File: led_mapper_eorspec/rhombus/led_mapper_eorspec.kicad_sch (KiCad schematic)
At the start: 1 part, among them J1 Conn_02x12_Top_Bottom

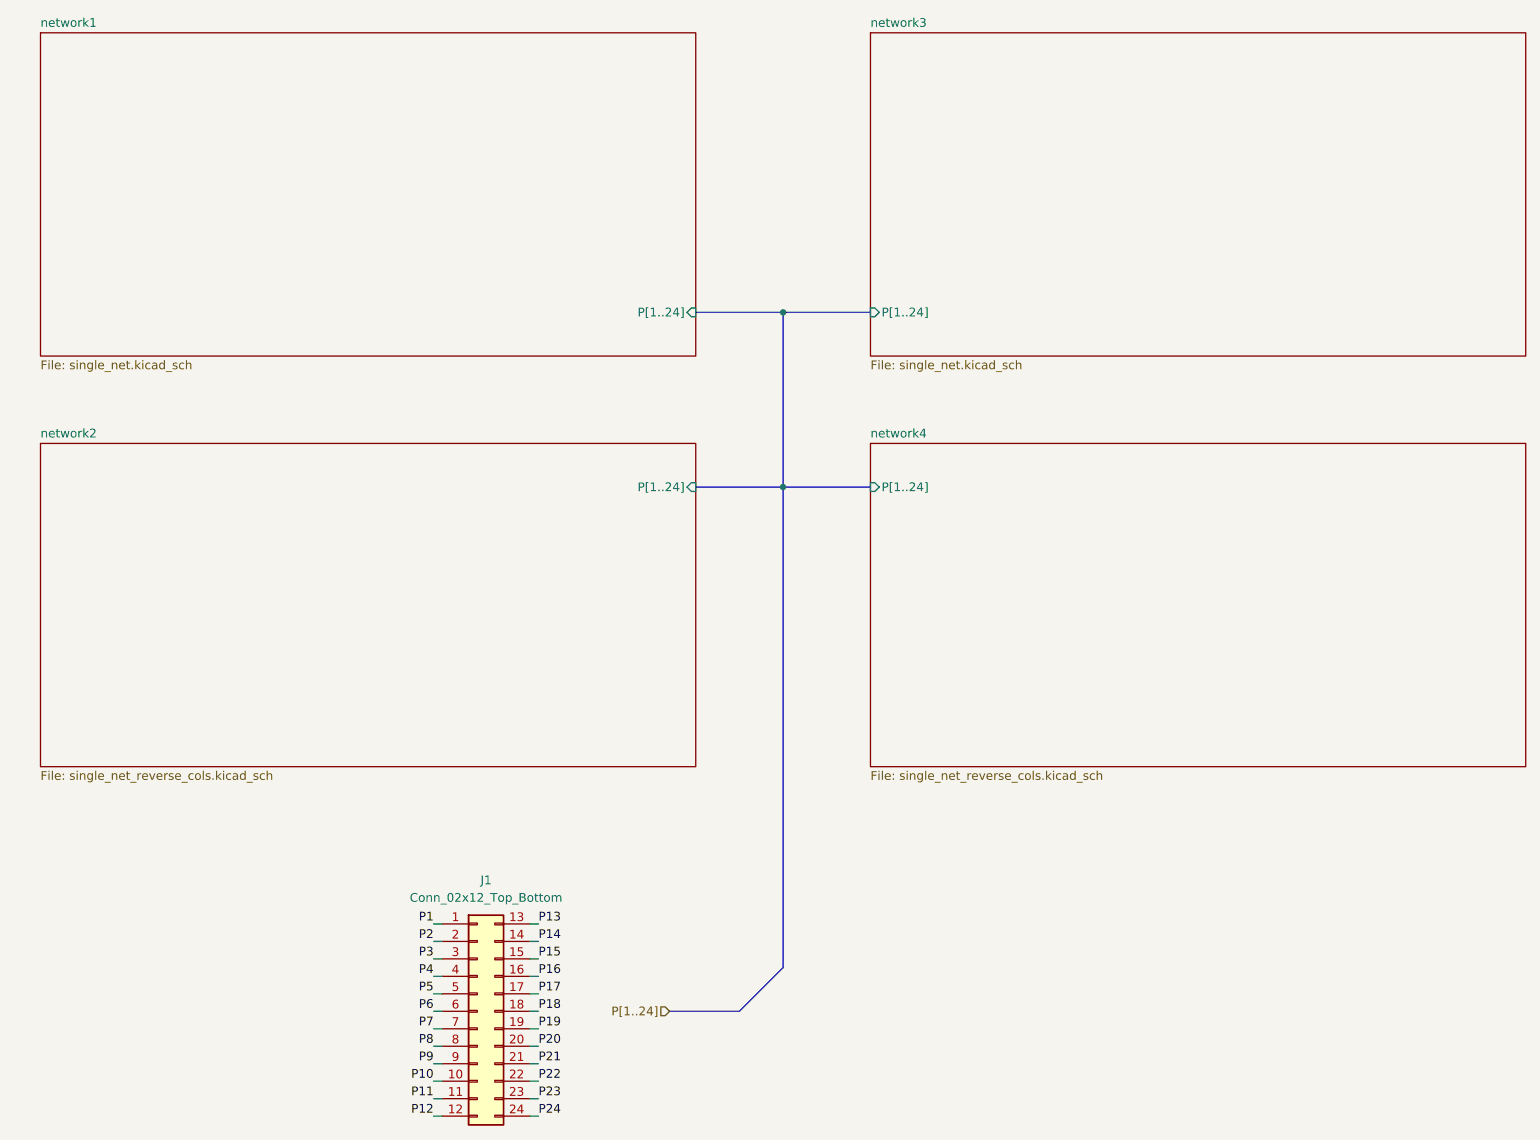
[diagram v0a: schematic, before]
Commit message: Complete single-net schematic, led placement and vertical tracks
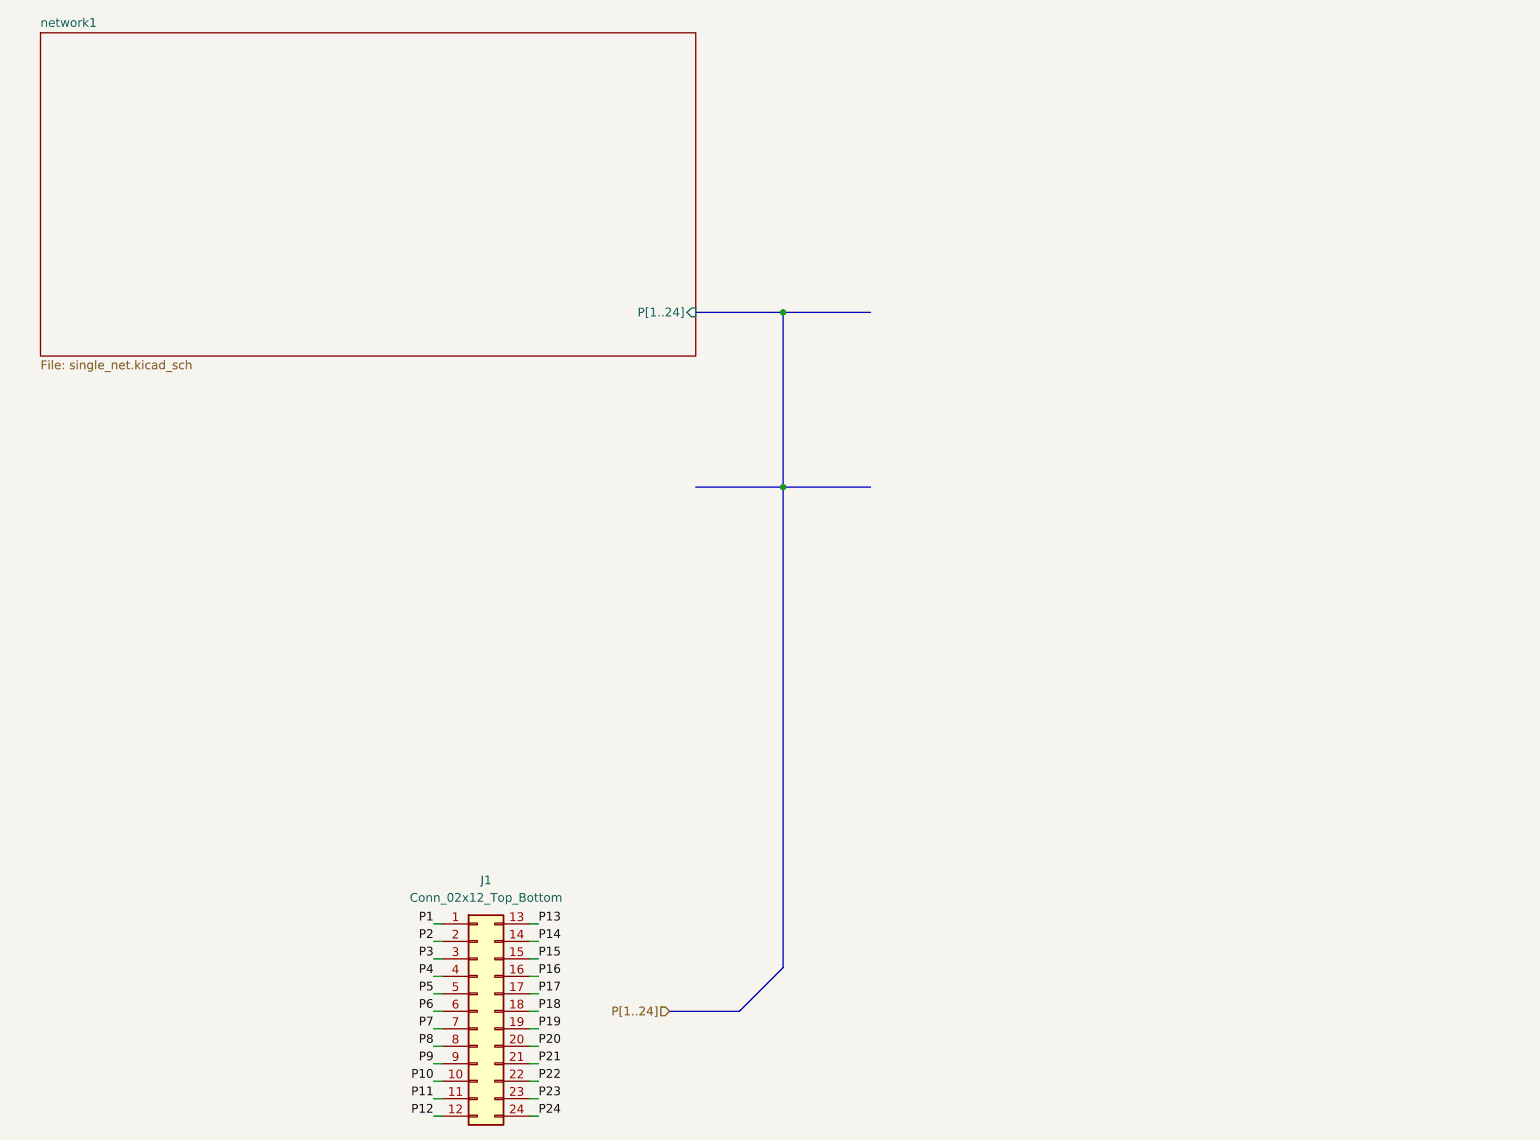
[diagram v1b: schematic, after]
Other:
- removed sheet network2
- removed sheet network3
- removed sheet network4
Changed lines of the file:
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@@
 (kicad_sch
-	(version 20231120)
+	(version 20260306)
 	(generator "eeschema")
-	(generator_version "8.0")
+	(generator_version "10.0")
 	(paper "A4")
 	(junction
@@
 		(at 107.95 171.45 0)
 		(unit 1)
+		(body_style 1)
+		(exclude_from_sim no)
+		(in_bom yes)
+		(on_board yes)
+		(in_pos_files yes)
+		(dnp no)
+		(fields_autoplaced yes)
+		(property "Reference" "J1"
+			(at 109.22 152.4 0)
+			(show_name no)
+			(do_not_autoplace no)
+			(effects
+				(font
+					(size 1.27 1.27)
+				)
+			)
+		)
+		(property "Value" "Conn_02x12_Top_Bottom"
+			(at 109.22 154.94 0)
+			(show_name no)
+			(do_not_autoplace no)
+			(effects
+				(font
+					(size 1.27 1.27)
+				)
+			)
+		)
+		(property "Footprint" "ccatlib:PinSocket_2x12_P2.54mm_Vertical_SMD_custom"
+			(at 107.95 171.45 0)
+			(hide yes)
+			(show_name no)
+			(do_not_autoplace no)
+			(effects
+				(font
+					(size 1.27 1.27)
+				)
+			)
+		)
+		(property "Datasheet" ""
+			(at 107.95 171.45 0)
+			(hide yes)
+			(show_name no)
+			(do_not_autoplace no)
+			(effects
+				(font
+					(size 1.27 1.27)
+				)
+			)
+		)
+		(property "Description" "Generic connector, double row, 02x12, top/bottom pin numbering scheme (row 1: 1...pins_per_row, row2: pins_per_row+1 ... num_pins), script generated (kicad-library-utils/schlib/autogen/connector/)"
+			(at 107.95 171.45 0)
+			(hide yes)
+			(show_name no)
+			(do_not_autoplace no)
+			(effects
+				(font
+					(size 1.27 1.27)
+				)
+			)
+		)
+		(property "LCSC Part #" "C19268781"
+			(at 107.95 171.45 0)
+			(hide yes)
+			(show_name no)
+			(do_not_autoplace no)
+			(effects
+				(font
+					(size 1.27 1.27)
+				)
+			)
+		)
+		(pin "9"
+		)
+		(pin "24"
+		)
+		(pin "12"
+		)
+		(pin "8"
+		)
+		(pin "1"
+		)
+		(pin "16"
+		)
+		(pin "22"
+		)
+		(pin "20"
+		)
+		(pin "5"
+		)
+		(pin "10"
+		)
+		(pin "15"
+		)
+		(pin "13"
+		)
+		(pin "19"
+		)
+		(pin "11"
+		)
+		(pin "2"
+		)
+		(pin "21"
+		)
+		(pin "23"
+		)
+		(pin "18"
+		)
+		(pin "17"
+		)
+		(pin "3"
+		)
+		(pin "14"
+		)
+		(pin "4"
+		)
+		(pin "6"
+		)
+		(pin "7"
+		)
+		(instances
+			(project "led_mapper_eorspec"
+				(path "/51b7e780-688f-494d-9172-4437a593740a"
+					(reference "J1")
+					(unit 1)
+				)
+			)
+		)
+	)
+	(sheet
+		(at 44.45 29.21)
+		(size 95.25 46.99)
 		(exclude_from_sim no)
 		(in_bom yes)
@@
 		(dnp no)
 		(fields_autoplaced yes)
-		(property "Reference" "J1"
-			(at 109.22 152.4 0)
-			(effects
-				(font
-					(size 1.27 1.27)
-				)
-			)
-		)
-		(property "Value" "Conn_02x12_Top_Bottom"
-			(at 109.22 154.94 0)
-			(effects
-				(font
-					(size 1.27 1.27)
-				)
-			)
-		)
-		(property "Footprint" "ccatlib:PinSocket_2x12_P2.54mm_Vertical_SMD_custom"
-			(at 107.95 171.45 0)
-			(effects
-				(font
-					(size 1.27 1.27)
-				)
-				(hide yes)
-			)
-		)
-		(property "Datasheet" "~"
-			(at 107.95 171.45 0)
-			(effects
-				(font
-					(size 1.27 1.27)
-				)
-				(hide yes)
-			)
-		)
-		(property "Description" "Generic connector, double row, 02x12, top/bottom pin numbering scheme (row 1: 1...pins_per_row, row2: pins_per_row+1 ... num_pins), script generated (kicad-library-utils/schlib/autogen/connector/)"
-			(at 107.95 171.45 0)
-			(effects
-				(font
-					(size 1.27 1.27)
-				)
-				(hide yes)
-			)
-		)
-		(property "LCSC Part #" "C19268781"
-			(at 107.95 171.45 0)
-			(effects
-				(font
-					(size 1.27 1.27)
-				)
-				(hide yes)
-			)
-		)
-		(pin "9"
-		)
-		(pin "24"
-		)
-		(pin "12"
-		)
-		(pin "8"
-		)
-		(pin "1"
-		)
-		(pin "16"
-		)
-		(pin "22"
-		)
-		(pin "20"
-		)
-		(pin "5"
-		)
-		(pin "10"
-		)
-		(pin "15"
-		)
-		(pin "13"
-		)
-		(pin "19"
-		)
-		(pin "11"
-		)
-		(pin "2"
-		)
-		(pin "21"
-		)
-		(pin "23"
-		)
-		(pin "18"
-		)
-		(pin "17"
-		)
-		(pin "3"
-		)
-		(pin "14"
-		)
-		(pin "4"
-		)
-		(pin "6"
-		)
-		(pin "7"
-		)
-		(instances
-			(project "led_mapper_850"
-				(path "/51b7e780-688f-494d-9172-4437a593740a"
-					(reference "J1")
-					(unit 1)
-				)
-			)
-		)
-	)
-	(sheet
-		(at 44.45 29.21)
-		(size 95.25 46.99)
-		(fields_autoplaced yes)
 		(stroke
 			(width 0.1524)
@@
 		)
 		(fill
-			(color 0 0 0 0.0000)
+			(color 0 0 0 0)
 		)
 		(property "Sheetname" "network1"
 			(at 44.45 28.4984 0)
+			(show_name no)
+			(do_not_autoplace no)
 			(effects
 				(font
@@
 		(property "Sheetfile" "single_net.kicad_sch"
 			(at 44.45 76.7846 0)
+			(show_name no)
+			(do_not_autoplace no)
 			(effects
 				(font
@@
 		)
 		(instances
-			(project "led_mapper_850"
+			(project "led_mapper_eorspec"
 				(path "/51b7e780-688f-494d-9172-4437a593740a"
 					(page "2")
-				)
-			)
-		)
-	)
-	(sheet
-		(at 165.1 29.21)
-		(size 95.25 46.99)
-		(fields_autoplaced yes)
-		(stroke
-			(width 0.1524)
-			(type solid)
-		)
-		(fill
-			(color 0 0 0 0.0000)
-		)
-		(property "Sheetname" "network3"
-			(at 165.1 28.4984 0)
-			(effects
-				(font
-					(size 1.27 1.27)
-				)
-				(justify left bottom)
-			)
-		)
-		(property "Sheetfile" "single_net.kicad_sch"
-			(at 165.1 76.7846 0)
-			(effects
-				(font
-					(size 1.27 1.27)
-				)
-				(justify left top)
-			)
-		)
-		(pin "P[1..24]" input
-			(at 165.1 69.85 180)
-			(effects
-				(font
-					(size 1.27 1.27)
-				)
-				(justify left)
-			)
-		)
-		(instances
-			(project "led_mapper_850"
-				(path "/51b7e780-688f-494d-9172-4437a593740a"
-					(page "4")
-				)
-			)
-		)
-	)
-	(sheet
-		(at 165.1 88.9)
-		(size 95.25 46.99)
-		(fields_autoplaced yes)
-		(stroke
-			(width 0.1524)
-			(type solid)
-		)
-		(fill
-			(color 0 0 0 0.0000)
-		)
-		(property "Sheetname" "network4"
-			(at 165.1 88.1884 0)
-			(effects
-				(font
-					(size 1.27 1.27)
-				)
-				(justify left bottom)
-			)
-		)
-		(property "Sheetfile" "single_net_reverse_cols.kicad_sch"
-			(at 165.1 136.4746 0)
-			(effects
-				(font
-					(size 1.27 1.27)
-				)
-				(justify left top)
-			)
-		)
-		(pin "P[1..24]" input
-			(at 165.1 95.25 180)
-			(effects
-				(font
-					(size 1.27 1.27)
-				)
-				(justify left)
-			)
-		)
-		(instances
-			(project "led_mapper_850"
-				(path "/51b7e780-688f-494d-9172-4437a593740a"
-					(page "5")
-				)
-			)
-		)
-	)
-	(sheet
-		(at 44.45 88.9)
-		(size 95.25 46.99)
-		(fields_autoplaced yes)
-		(stroke
-			(width 0.1524)
-			(type solid)
-		)
-		(fill
-			(color 0 0 0 0.0000)
-		)
-		(property "Sheetname" "network2"
-			(at 44.45 88.1884 0)
-			(effects
-				(font
-					(size 1.27 1.27)
-				)
-				(justify left bottom)
-			)
-		)
-		(property "Sheetfile" "single_net_reverse_cols.kicad_sch"
-			(at 44.45 136.4746 0)
-			(effects
-				(font
-					(size 1.27 1.27)
-				)
-				(justify left top)
-			)
-		)
-		(pin "P[1..24]" input
-			(at 139.7 95.25 0)
-			(effects
-				(font
-					(size 1.27 1.27)
-				)
-				(justify right)
-			)
-		)
-		(instances
-			(project "led_mapper_850"
-				(path "/51b7e780-688f-494d-9172-4437a593740a"
-					(page "3")
 				)
 			)
@@
 		)
 	)
+	(embedded_fonts no)
 )

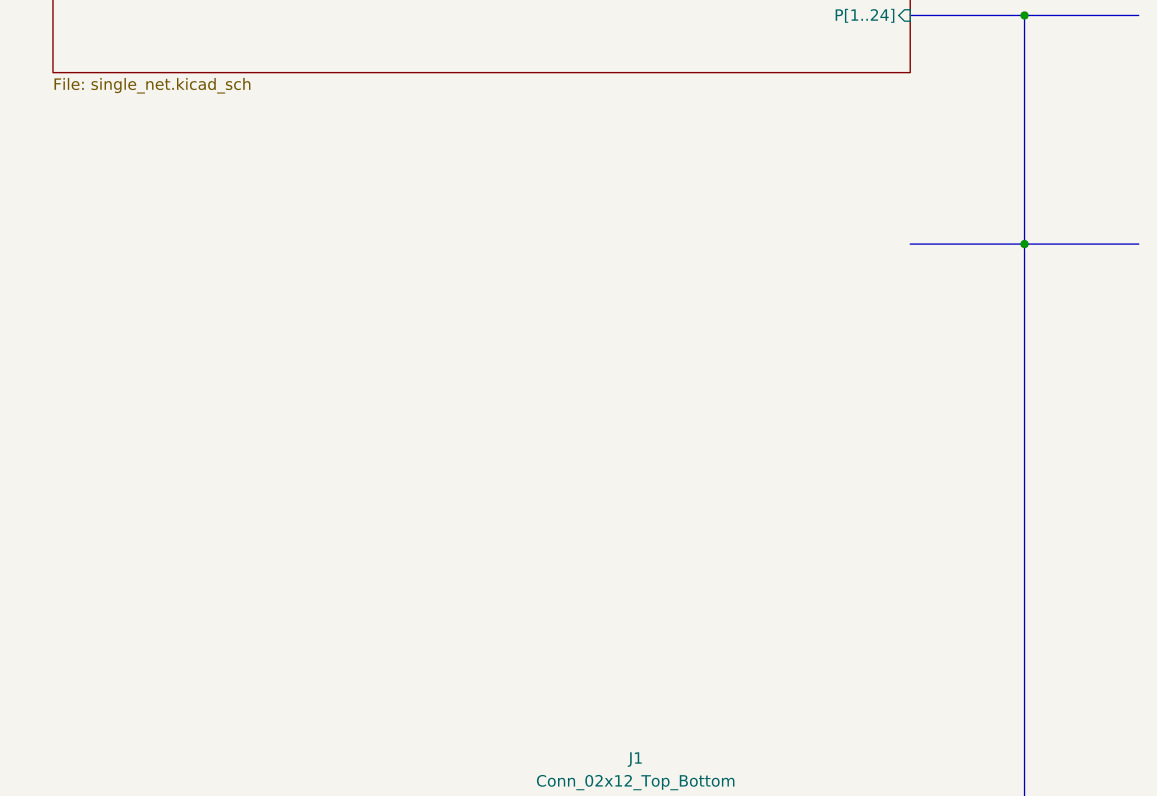
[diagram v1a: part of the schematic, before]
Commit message: Add second network to PCB
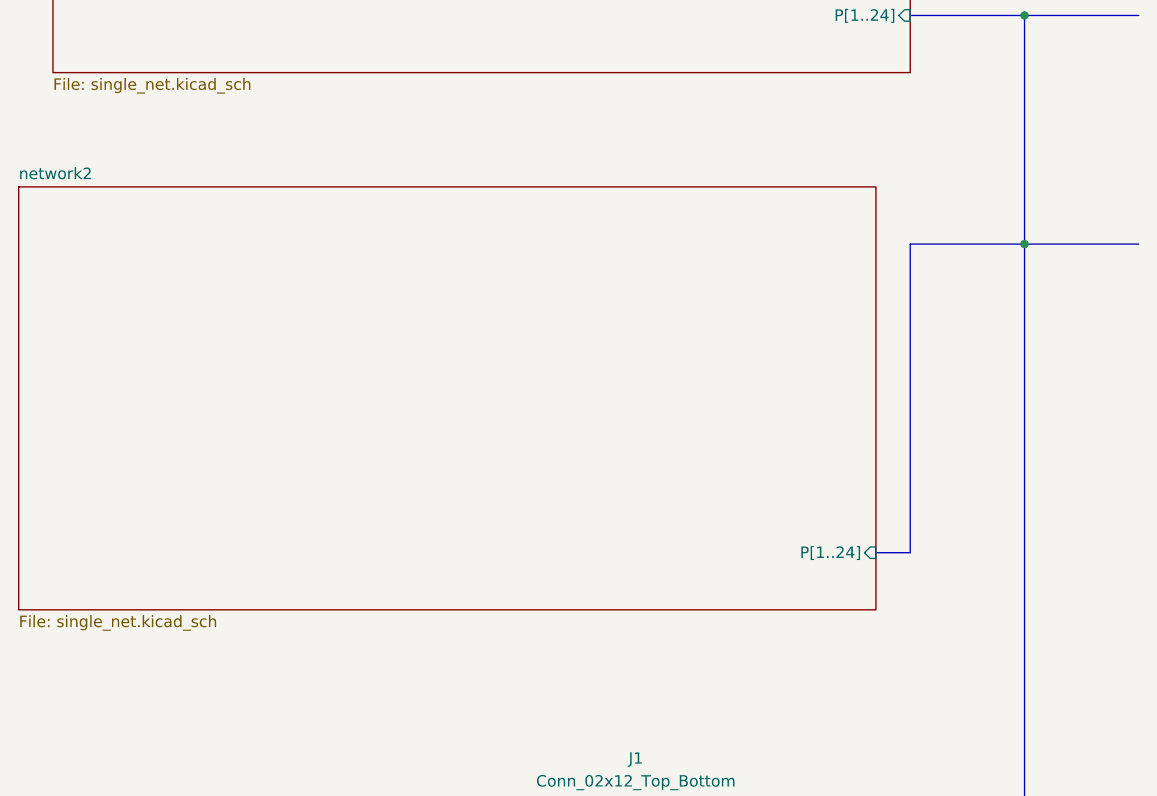
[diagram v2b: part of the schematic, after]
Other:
- added sheet network2 (single_net.kicad_sch)
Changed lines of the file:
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@@
+		)
+	)
+	(bus
+		(pts
+			(xy 139.7 95.25) (xy 139.7 129.54)
+		)
+		(stroke
+			(width 0)
+			(type default)
 		)
 	)
@@
 	(bus
 		(pts
-			(xy 139.7 95.25) (xy 152.4 95.25)
+			(xy 152.4 95.25) (xy 139.7 95.25)
 		)
 		(stroke
@@
 		(pts
 			(xy 101.6 186.69) (xy 102.87 186.69)
+		)
+		(stroke
+			(width 0)
+			(type default)
+		)
+	)
+	(bus
+		(pts
+			(xy 139.7 129.54) (xy 135.89 129.54)
 		)
 		(stroke
@@
 				)
 			)
+		)
+	)
+	(sheet
+		(at 40.64 88.9)
+		(size 95.25 46.99)
+		(exclude_from_sim no)
+		(in_bom yes)
+		(on_board yes)
+		(dnp no)
+		(fields_autoplaced yes)
+		(stroke
+			(width 0.1524)
+			(type solid)
+		)
+		(fill
+			(color 0 0 0 0)
+		)
+		(property "Sheetname" "network2"
+			(at 40.64 88.1884 0)
+			(show_name no)
+			(do_not_autoplace no)
+			(effects
+				(font
+					(size 1.27 1.27)
+				)
+				(justify left bottom)
+			)
+		)
+		(property "Sheetfile" "single_net.kicad_sch"
+			(at 40.64 136.4746 0)
+			(show_name no)
+			(do_not_autoplace no)
+			(effects
+				(font
+					(size 1.27 1.27)
+				)
+				(justify left top)
+			)
+		)
+		(pin "P[1..24]" input
+			(at 135.89 129.54 0)
+			(effects
+				(font
+					(size 1.27 1.27)
+				)
+				(justify right)
+			)
+		)
+		(instances
+			(project "led_mapper_eorspec"
+				(path "/51b7e780-688f-494d-9172-4437a593740a"
+					(page "3")
+				)
+			)
